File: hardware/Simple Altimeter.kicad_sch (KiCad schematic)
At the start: 41 parts, among them J1 USB_C_Receptacle_USB2.0, J2 Conn_01x05_Pin, Q2 DMN3607LW, Q3 Q_NMOS_GDS, SW2 SW_Push, U1 WS4518, U2 BMP280, U3 W25Q16JVUXIQ, U4 STM32F042G6Ux, U5 XB6042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

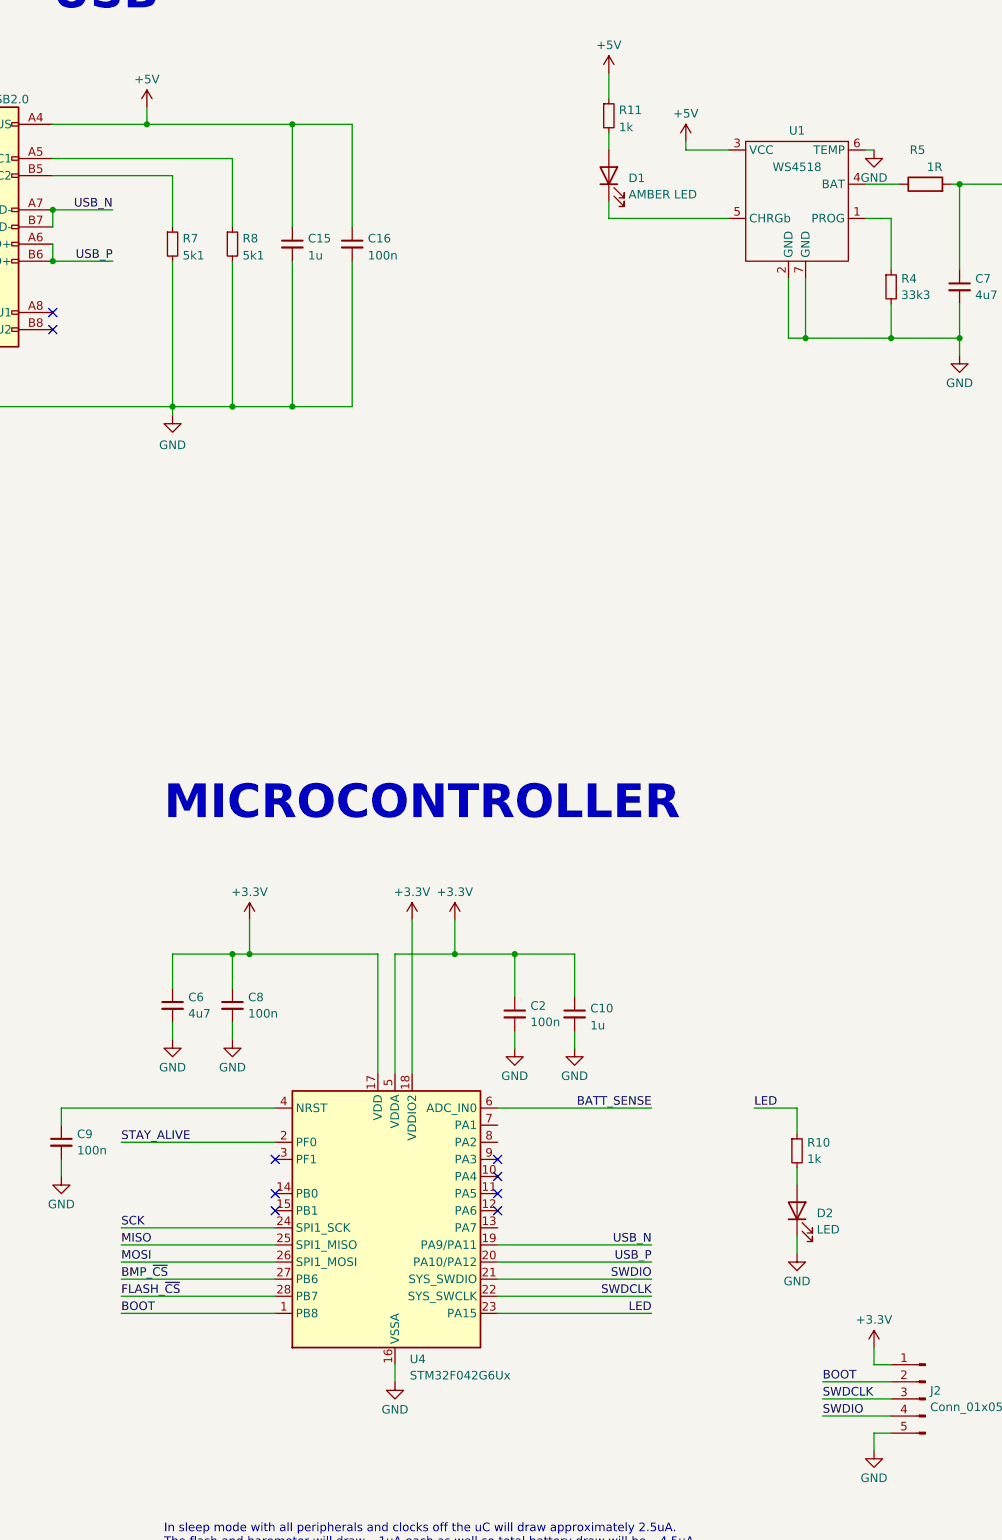
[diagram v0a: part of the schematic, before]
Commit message: Fixed boot pin and strengthened teather loop. Added BOMs and manufacturing data.
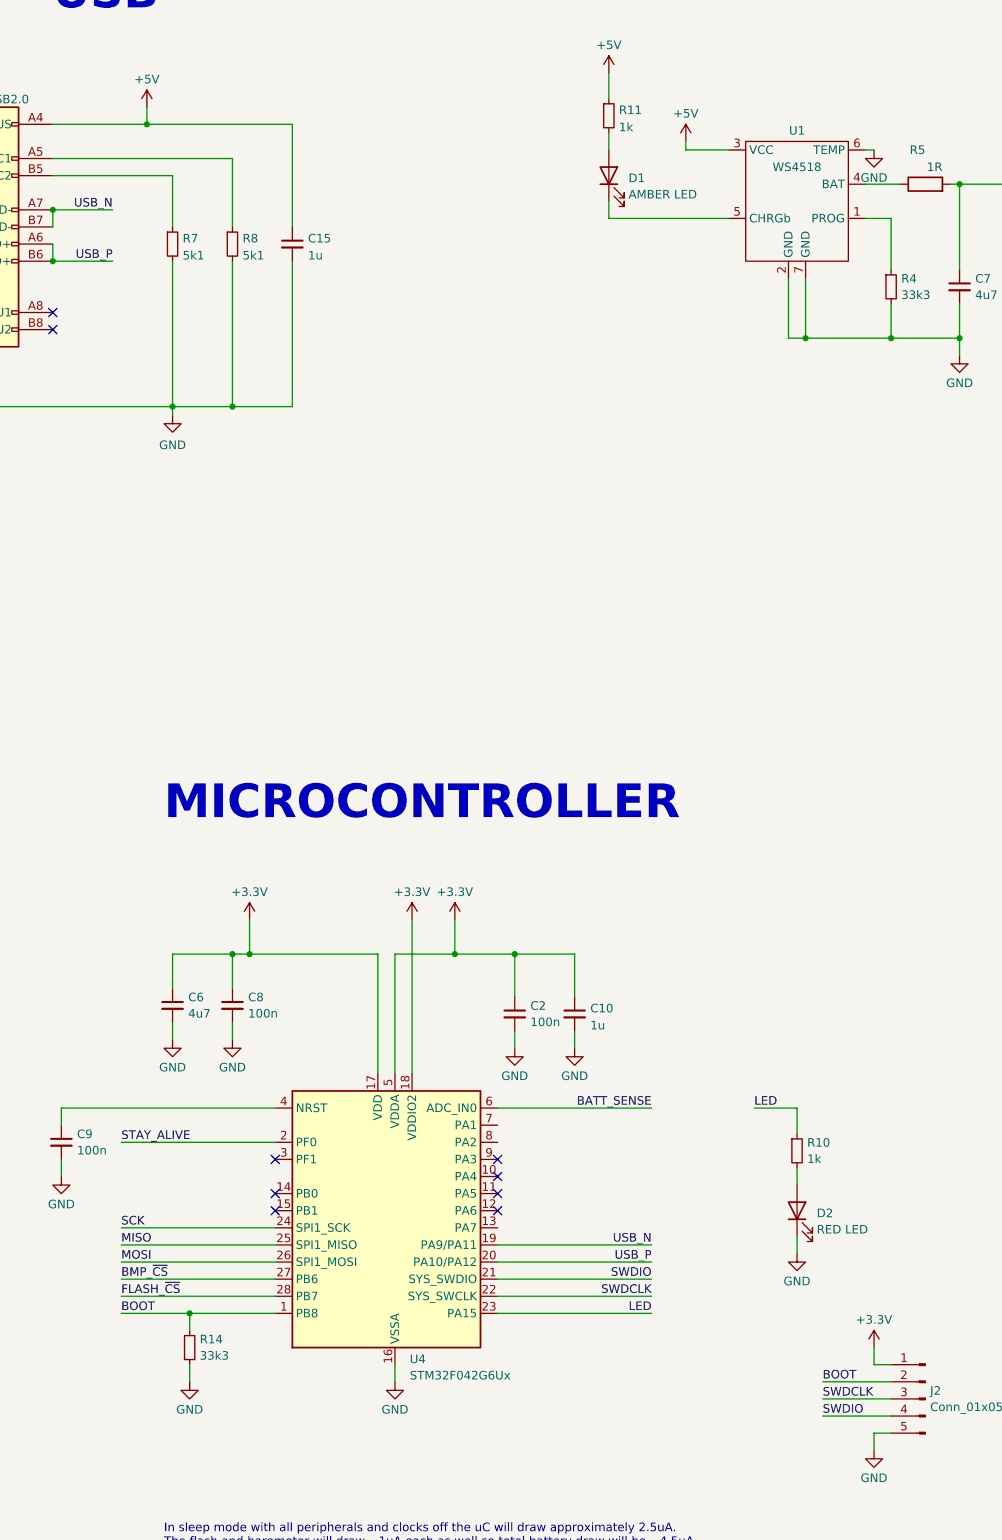
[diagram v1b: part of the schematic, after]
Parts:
- removed C16: 100n, Capacitor_SMD:C_0402_1005Metric, symbol Device:C_Small
- added R14: 33k3, Resistor_SMD:R_0402_1005Metric, symbol Device:R_Small
- D2: value LED -> RED LED
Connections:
- net BOOT: now also R14.1
- net GND: now also R14.2
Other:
- company: (none) -> Blueskin Design Ltd
- title: (none) -> SimpleAlt
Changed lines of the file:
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@@
 (kicad_sch (version 20230121) (generator eeschema)
   (paper "A3")
+  (title_block
+    (title "SimpleAlt")
+    (date "2024-06-22")
+    (rev "2")
+    (company "Blueskin Design Ltd")
+    (comment 1 "(C) 2024 Michael Turner")
+  )
   (junction (at 332.74 53.34) (diameter 0) (color 0 0 0 0)
   )
-  (junction (at 88.9 96.52) (diameter 0) (color 0 0 0 0)
+  (junction (at 73.66 231.14) (diameter 0) (color 0 0 0 0)
   )
   (junction (at 227.33 73.66) (diameter 0) (color 0 0 0 0)
@@
   )
   (junction (at 222.25 73.66) (diameter 0) (color 0 0 0 0)
-  )
-  (junction (at 88.9 54.61) (diameter 0) (color 0 0 0 0)
   )
   (no_connect (at 86.36 213.36))
@@
     (stroke (width 0) (type default))
   )
-  (wire (pts (xy 88.9 96.52) (xy 97.79 96.52))
+  (wire (pts (xy 73.66 231.14) (xy 73.66 233.68))
     (stroke (width 0) (type default))
   )
@@
     (stroke (width 0) (type default))
   )
-  (wire (pts (xy 97.79 74.93) (xy 97.79 96.52))
-    (stroke (width 0) (type default))
-  )
   (wire (pts (xy 187.96 63.5) (xy 200.66 63.5))
     (stroke (width 0) (type default))
@@
     (stroke (width 0) (type default))
   )
-  (wire (pts (xy 97.79 54.61) (xy 97.79 69.85))
-    (stroke (width 0) (type default))
-  )
   (wire (pts (xy 222.25 63.5) (xy 227.33 63.5))
     (stroke (width 0) (type default))
@@
     (stroke (width 0) (type default))
   )
-  (wire (pts (xy 63.5 231.14) (xy 86.36 231.14))
+  (wire (pts (xy 63.5 231.14) (xy 73.66 231.14))
     (stroke (width 0) (type default))
   )
@@
     (stroke (width 0) (type default))
   )
+  (wire (pts (xy 73.66 231.14) (xy 86.36 231.14))
+    (stroke (width 0) (type default))
+  )
   (wire (pts (xy 167.64 243.84) (xy 177.8 243.84))
     (stroke (width 0) (type default))
@@
     (stroke (width 0) (type default))
   )
+  (wire (pts (xy 73.66 238.76) (xy 73.66 241.3))
+    (stroke (width 0) (type default))
+  )
   (wire (pts (xy 53.34 62.23) (xy 71.12 62.23))
     (stroke (width 0) (type default))
@@
   )
   (wire (pts (xy 227.33 71.12) (xy 227.33 73.66))
-    (stroke (width 0) (type default))
-  )
-  (wire (pts (xy 88.9 54.61) (xy 97.79 54.61))
     (stroke (width 0) (type default))
   )
@@
       (effects (font (size 1.27 1.27)) (justify right))
     )
-    (property "Value" "LED" (at 166.751 218.6996 90)
+    (property "Value" "RED LED" (at 166.751 218.6996 90)
       (effects (font (size 1.27 1.27)) (justify right))
     )
@@
     )
   )
-  (symbol (lib_id "Device:C_Small") (at 97.79 72.39 0) (unit 1)
-    (in_bom yes) (on_board yes) (dnp no) (fields_autoplaced)
-    (property "Reference" "C16" (at 100.1141 71.5616 0)
-      (effects (font (size 1.27 1.27)) (justify left))
-    )
-    (property "Value" "100n" (at 100.1141 74.0985 0)
-      (effects (font (size 1.27 1.27)) (justify left))
-    )
-    (property "Footprint" "Capacitor_SMD:C_0402_1005Metric" (at 97.79 72.39 0)
-      (effects (font (size 1.27 1.27)) hide)
-    )
-    (property "Datasheet" "~" (at 97.79 72.39 0)
-      (effects (font (size 1.27 1.27)) hide)
-    )
-    (property "JLC Part Number" "" (at 97.79 72.39 0)
-      (effects (font (size 1.27 1.27)) hide)
-    )
-    (pin "1")
-    (pin "2")
-    (instances
-      (project "Simple Altimeter"
-        (path "/80f3d735-68fa-4a00-8377-fe541c005eac"
-          (reference "C16") (unit 1)
+  (symbol (lib_id "Device:R_Small") (at 73.66 236.22 0) (unit 1)
+    (in_bom yes) (on_board yes) (dnp no) (fields_autoplaced)
+    (property "Reference" "R14" (at 75.1586 235.0079 0)
+      (effects (font (size 1.27 1.27)) (justify left))
+    )
+    (property "Value" "33k3" (at 75.1586 237.4321 0)
+      (effects (font (size 1.27 1.27)) (justify left))
+    )
+    (property "Footprint" "Resistor_SMD:R_0402_1005Metric" (at 73.66 236.22 0)
+      (effects (font (size 1.27 1.27)) hide)
+    )
+    (property "Datasheet" "~" (at 73.66 236.22 0)
+      (effects (font (size 1.27 1.27)) hide)
+    )
+    (property "JLC Part Number" "C3013567" (at 73.66 236.22 0)
+      (effects (font (size 1.27 1.27)) hide)
+    )
+    (pin "1")
+    (pin "2")
+    (instances
+      (project "Simple Altimeter"
+        (path "/80f3d735-68fa-4a00-8377-fe541c005eac"
+          (reference "R14") (unit 1)
         )
       )
@@
         )
       )
+    )
+  )
+  (symbol (lib_id "power:GND") (at 73.66 241.3 0) (mirror y) (unit 1)
+    (in_bom yes) (on_board yes) (dnp no) (fields_autoplaced)
+    (property "Reference" "#PWR020" (at 73.66 247.65 0)
+      (effects (font (size 1.27 1.27)) hide)
+    )
+    (property "Value" "GND" (at 73.66 245.4331 0)
+      (effects (font (size 1.27 1.27)))
+    )
+    (property "Footprint" "" (at 73.66 241.3 0)
+      (effects (font (size 1.27 1.27)) hide)
+    )
+    (property "Datasheet" "" (at 73.66 241.3 0)
+      (effects (font (size 1.27 1.27)) hide)
+    )
+    (pin "1")
+    (instances
+      (project "Simple Altimeter"
+        (path "/80f3d735-68fa-4a00-8377-fe541c005eac"
+          (reference "#PWR020") (unit 1)
+        )
+      )

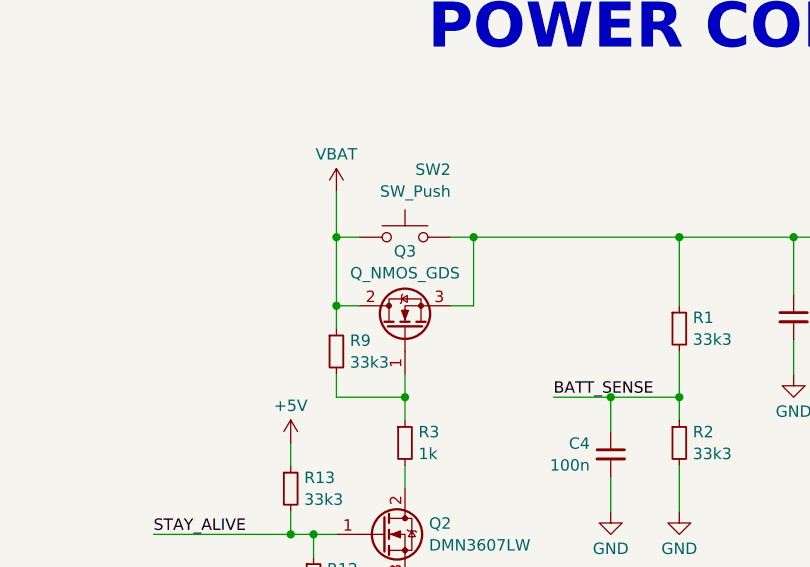
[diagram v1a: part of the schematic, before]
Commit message: Corrected Q1 schematic symbol (was NMOS, now correctly showing PMOS)
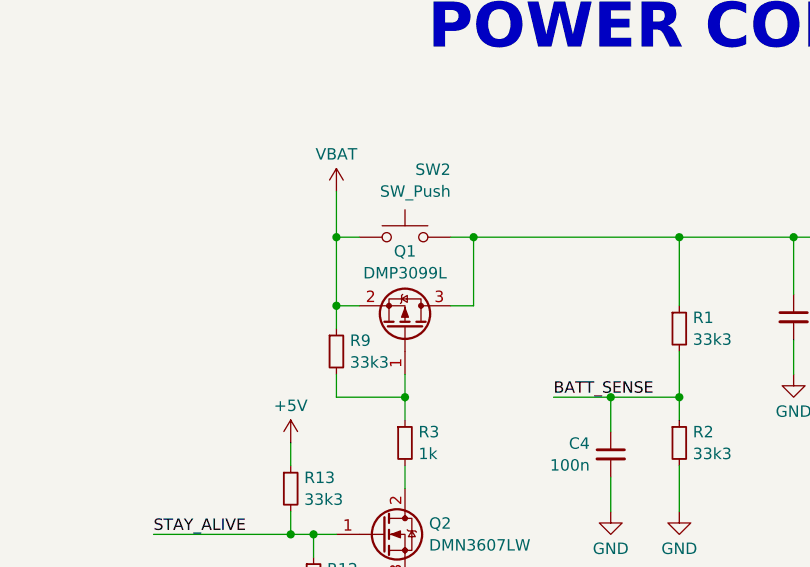
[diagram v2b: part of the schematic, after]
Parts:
- removed Q3: Q_NMOS_GDS, Package_TO_SOT_SMD:SOT-323_SC-70, symbol Device:Q_NMOS_GDS
- added Q1: DMP3099L, Package_TO_SOT_SMD:SOT-323_SC-70, symbol Device:Q_PMOS_GSD
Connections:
- net VBAT: now also Q1.2 (S)
- net at C1.1, R1.1, SW2.1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: now also Q1.3 (D)
- net at R3.1, R9.2: now also Q1.1 (G)
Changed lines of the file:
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@@
-    )
-  )
-  (symbol (lib_id "Device:Q_NMOS_GDS") (at 302.26 63.5 90) (unit 1)
-    (in_bom yes) (on_board yes) (dnp no)
-    (property "Reference" "Q3" (at 302.26 54.9107 90)
-      (effects (font (size 1.27 1.27)))
-    )
-    (property "Value" "Q_NMOS_GDS" (at 302.26 57.3349 90)
-      (effects (font (size 1.27 1.27)))
-    )
-    (property "Footprint" "Package_TO_SOT_SMD:SOT-323_SC-70" (at 299.72 58.42 0)
-      (effects (font (size 1.27 1.27)) hide)
-    )
-    (property "Datasheet" "~" (at 302.26 63.5 0)
-      (effects (font (size 1.27 1.27)) hide)
-    )
-    (pin "2")
-    (pin "3")
-    (pin "1")
-    (instances
-      (project "Simple Altimeter"
-        (path "/80f3d735-68fa-4a00-8377-fe541c005eac"
-          (reference "Q3") (unit 1)
-        )
-      )
     )
   )
@@
         )
       )
+    )
+  )
+  (symbol (lib_id "Device:Q_PMOS_GSD") (at 302.26 63.5 270) (mirror x) (unit 1)
+    (in_bom yes) (on_board yes) (dnp no) (fields_autoplaced)
+    (property "Reference" "Q1" (at 302.26 54.9107 90)
+      (effects (font (size 1.27 1.27)))
+    )
+    (property "Value" "DMP3099L" (at 302.26 57.3349 90)
+      (effects (font (size 1.27 1.27)))
+    )
+    (property "Footprint" "Package_TO_SOT_SMD:SOT-323_SC-70" (at 304.8 58.42 0)
+      (effects (font (size 1.27 1.27)) hide)
+    )
+    (property "Datasheet" "~" (at 302.26 63.5 0)
+      (effects (font (size 1.27 1.27)) hide)
+    )
+    (pin "1")
+    (pin "3")
+    (pin "2")
+    (instances
+      (project "Simple Altimeter"
+        (path "/80f3d735-68fa-4a00-8377-fe541c005eac"
+          (reference "Q1") (unit 1)
+        )
+      )

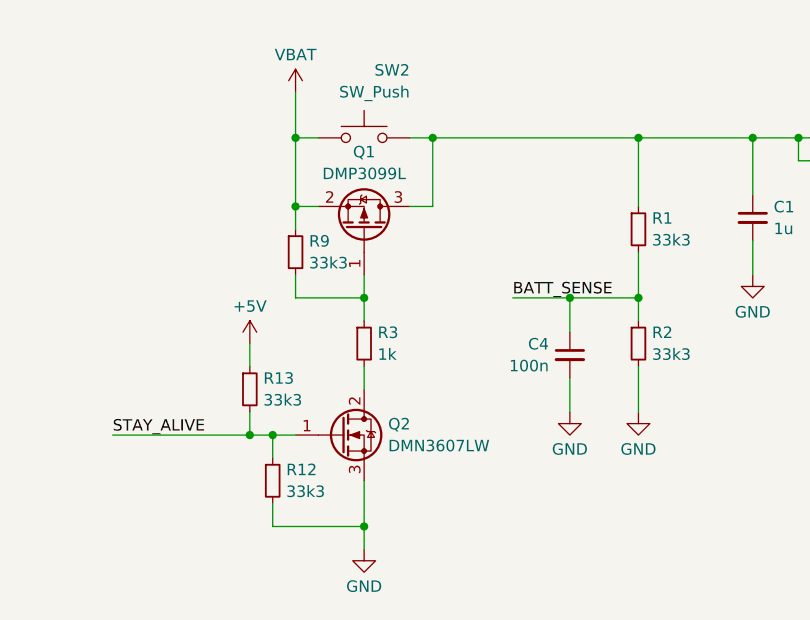
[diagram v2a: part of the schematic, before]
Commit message: Corrected Q2 part number.
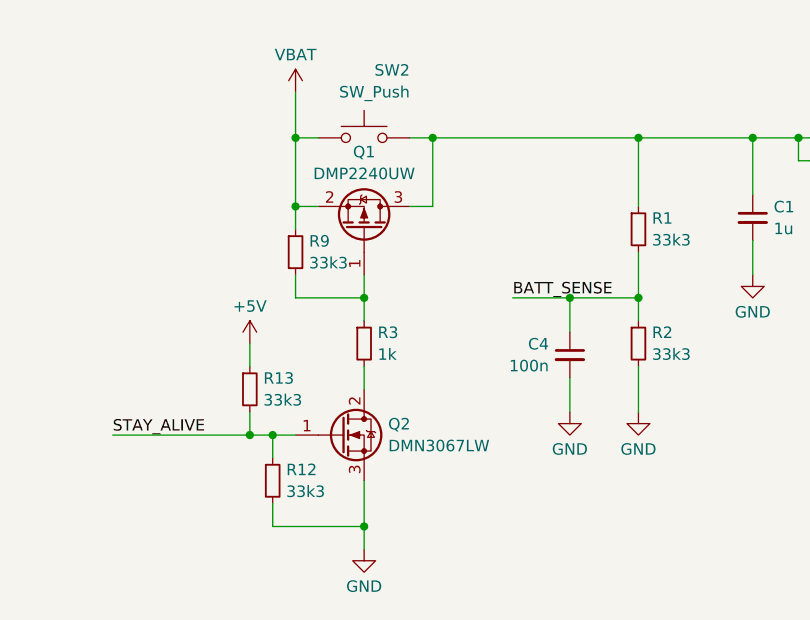
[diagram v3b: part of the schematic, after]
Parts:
- Q1: value DMP3099L -> DMP2240UW
- Q2: value DMN3607LW -> DMN3067LW
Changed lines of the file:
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@@
       (effects (font (size 1.27 1.27)))
     )
-    (property "Value" "DMP3099L" (at 302.26 57.3349 90)
+    (property "Value" "DMP2240UW" (at 302.26 57.3349 90)
       (effects (font (size 1.27 1.27)))
     )
@@
       (effects (font (size 1.27 1.27)) (justify left))
     )
-    (property "Value" "DMN3607LW" (at 304.927 87.5721 0)
+    (property "Value" "DMN3067LW" (at 304.927 87.5721 0)
       (effects (font (size 1.27 1.27)) (justify left))
     )

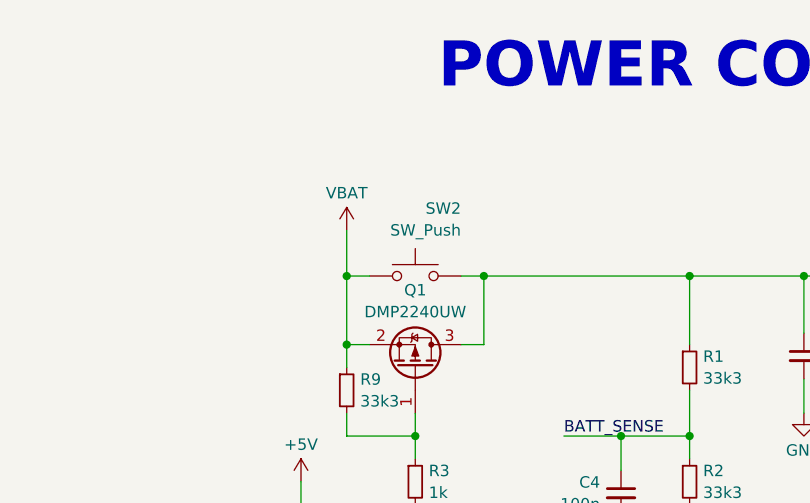
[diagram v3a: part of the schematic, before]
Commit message: updated button part number
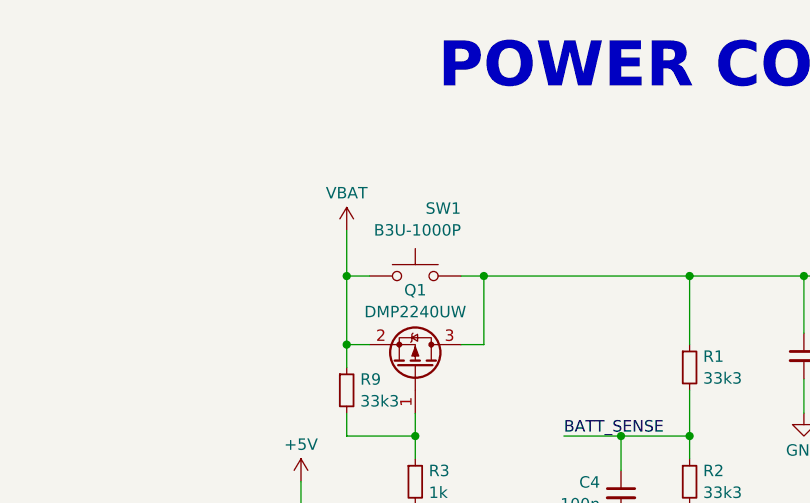
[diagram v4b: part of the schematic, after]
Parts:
- SW1: renamed from SW2; value SW_Push -> B3U-1000P
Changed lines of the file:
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@@
   (symbol (lib_id "Switch:SW_Push") (at 302.26 53.34 0) (mirror y) (unit 1)
     (in_bom yes) (on_board yes) (dnp no)
-    (property "Reference" "SW2" (at 307.34 45.8358 0)
+    (property "Reference" "SW1" (at 307.34 45.8358 0)
       (effects (font (size 1.27 1.27)) (justify left))
     )
-    (property "Value" "SW_Push" (at 307.34 48.26 0)
+    (property "Value" "B3U-1000P" (at 307.34 48.26 0)
       (effects (font (size 1.27 1.27)) (justify left))
     )
@@
       (project "Simple Altimeter"
         (path "/80f3d735-68fa-4a00-8377-fe541c005eac"
-          (reference "SW2") (unit 1)
+          (reference "SW1") (unit 1)
         )
       )
